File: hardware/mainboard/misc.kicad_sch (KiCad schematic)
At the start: 15 parts

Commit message: More stuff
Signed-off-by: David Shah <dave@ds0.me>
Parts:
- added D? (x2): LED_Small, symbol Device:LED_Small
- added Q?: 2N7002, Package_TO_SOT_SMD:SOT-23, symbol Transistor_FET:2N7002
- added R? (x2): 1k, symbol Device:R_Small
- added R? (x2): 10k, symbol Device:R_Small
- R? (x3): value 1k -> 220
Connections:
- net +3V3: now also R?.1, R?.1, R?.1
- net FLASH_CLK: now also R?.1
- net GND: now also D?.1 (K), Q?.2 (S), R?.2
- new net: D?.2 (A), R?.2 (x2)
- new net: D?.1 (K), Q?.3 (D)
- new net DONE: Q?.1 (G), R?.2
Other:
- moved on the sheet: D?, R?

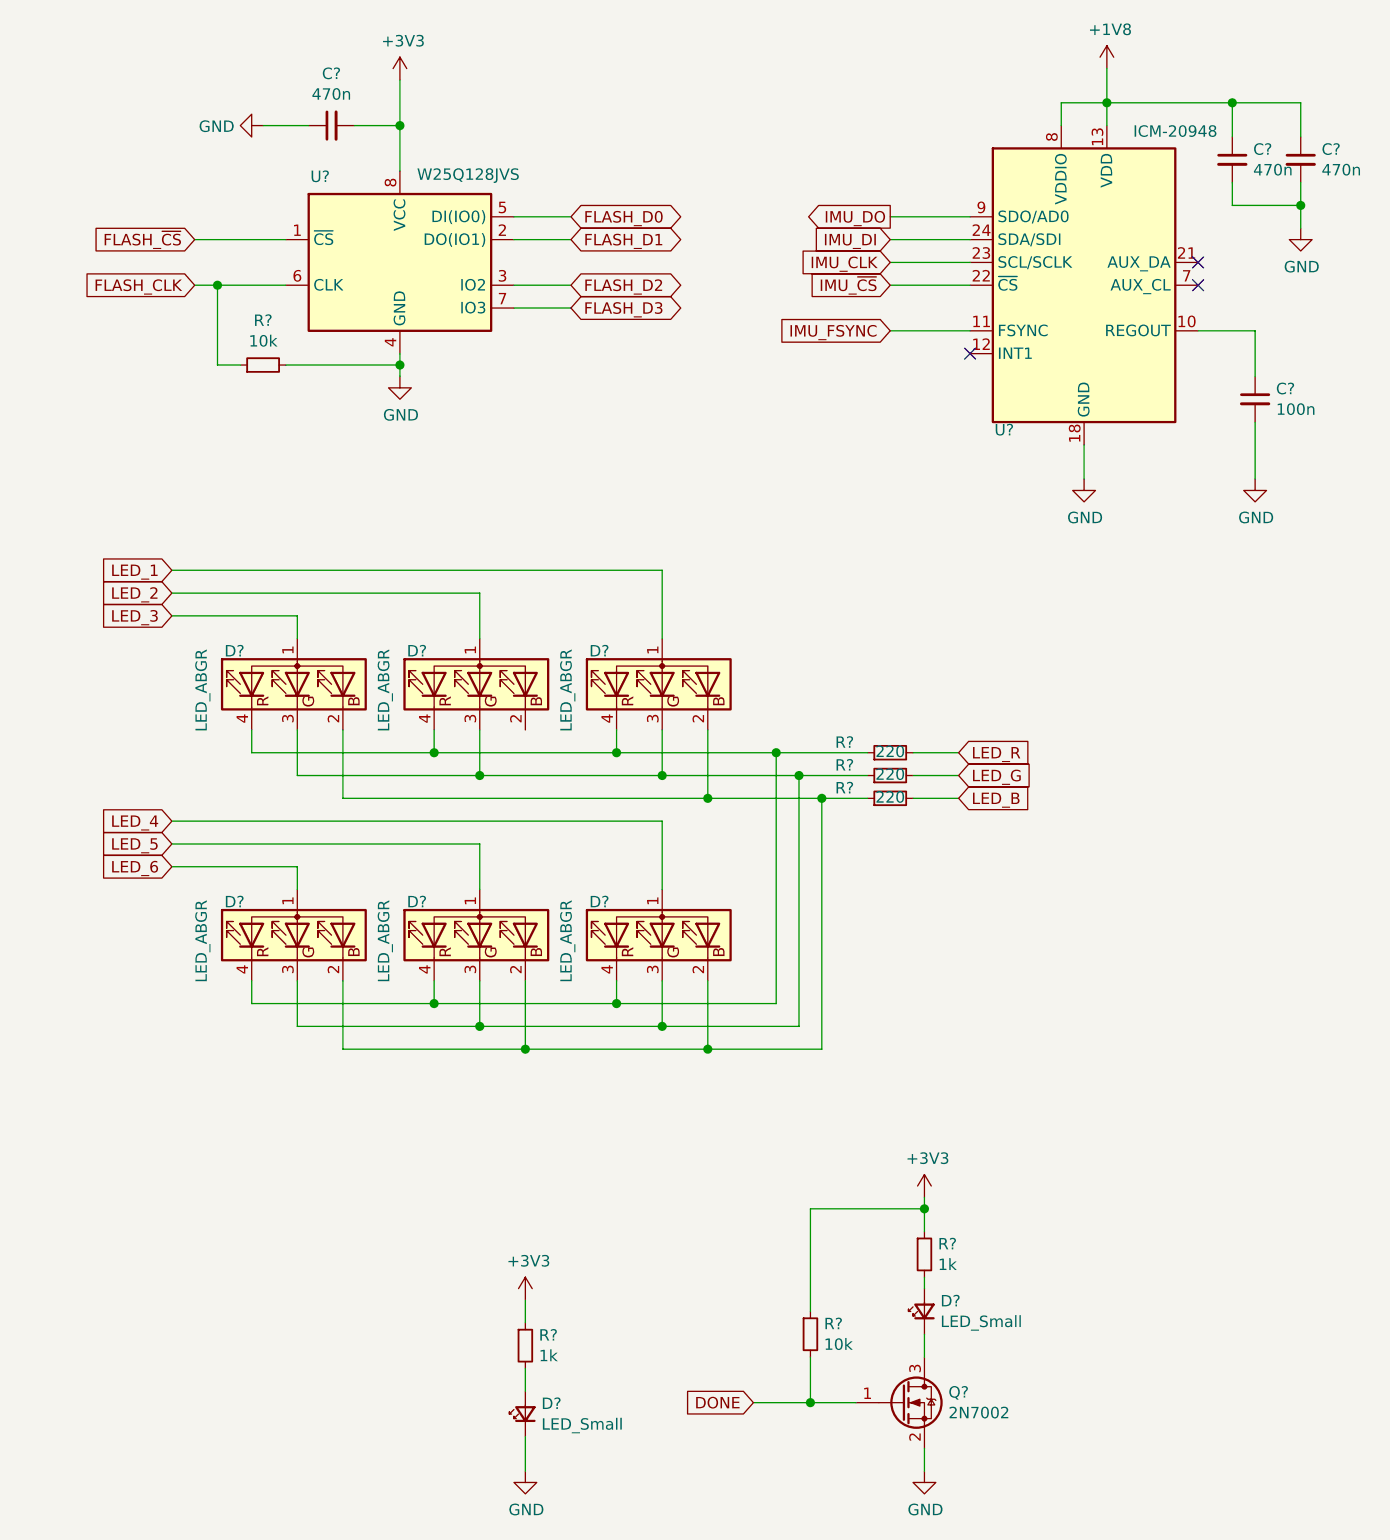
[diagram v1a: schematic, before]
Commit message: Annotate and assign some footpints
Signed-off-by: David Shah <dave@ds0.me>
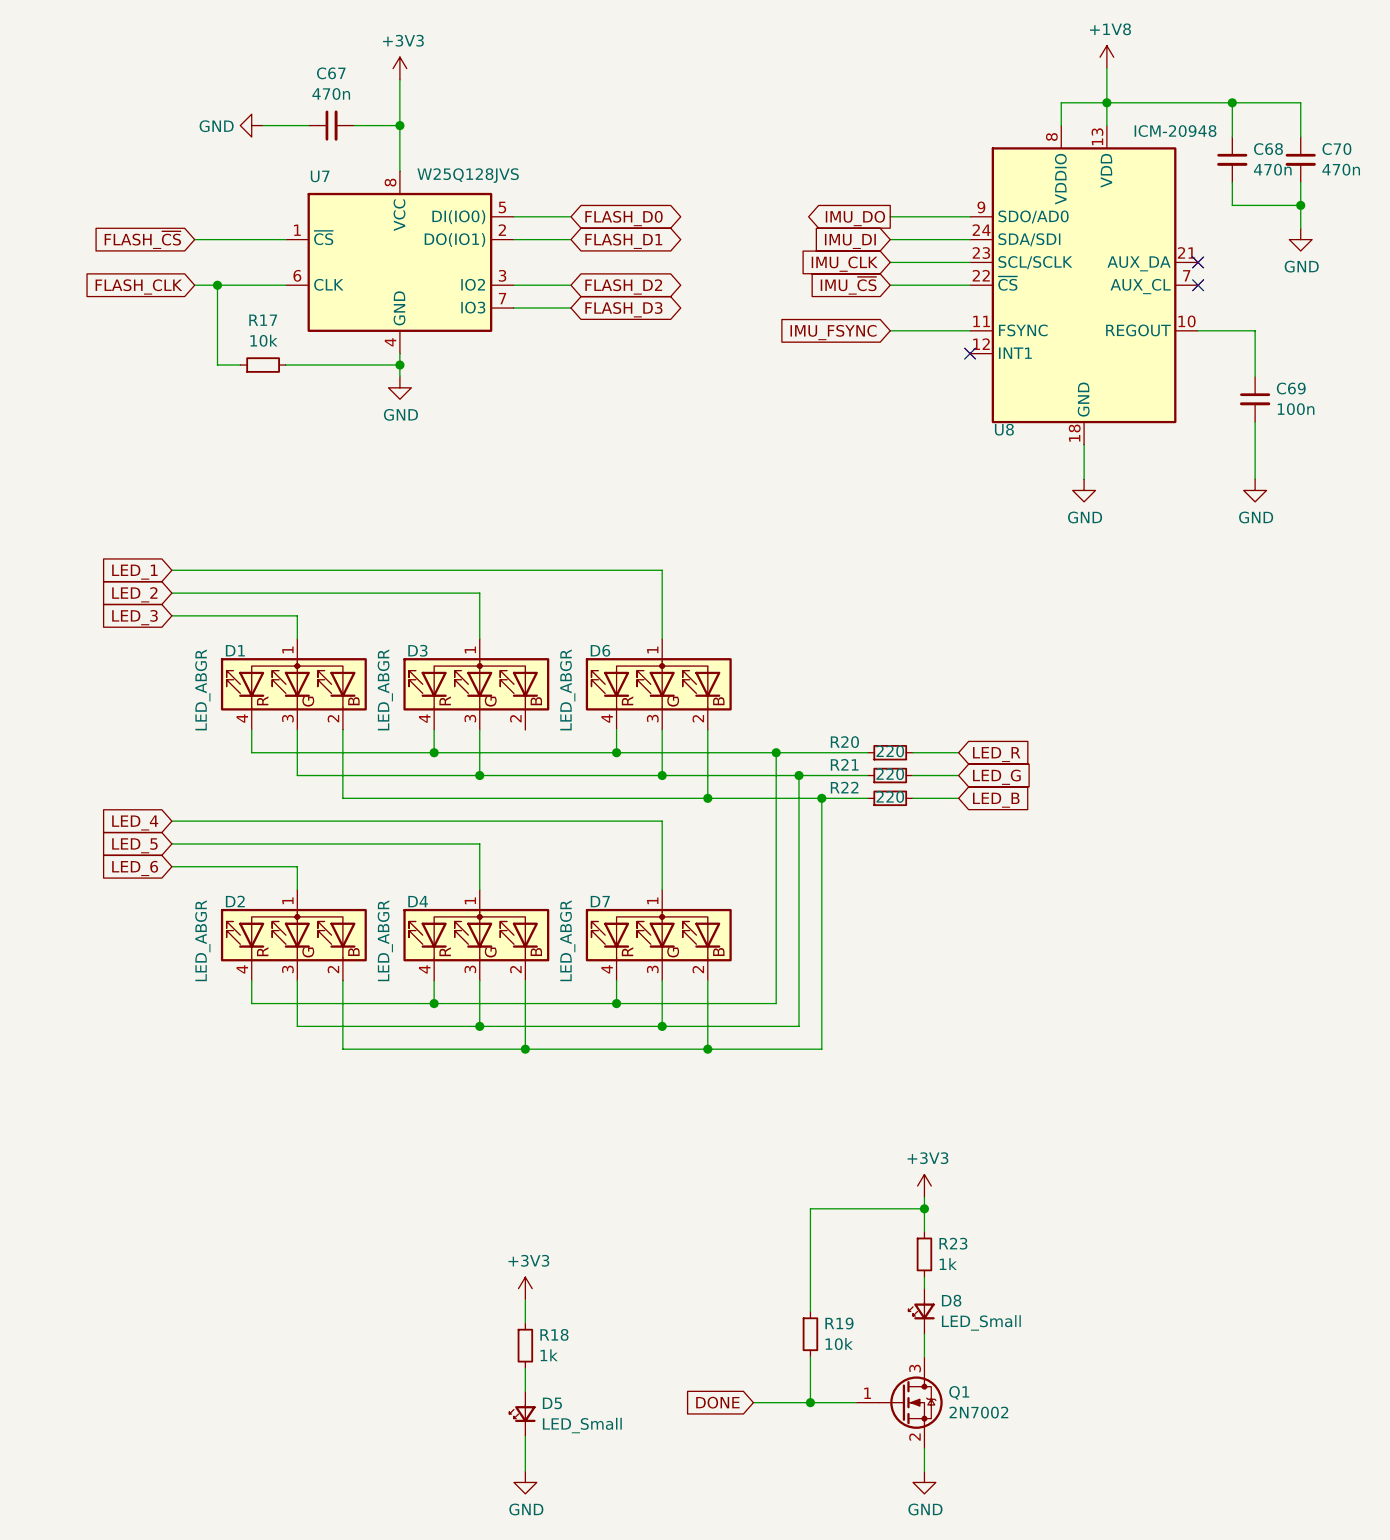
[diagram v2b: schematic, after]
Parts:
- C67, C68, C69, C70: renamed from C?; footprint (none) -> Capacitor_SMD:C_0402_1005Metric
- D1, D2, D3, D4, D6, D7: renamed from D?; footprint (none) -> LED_SMD:LED_Cree-PLCC4_2x2mm_CW
- D5, D8: renamed from D?; footprint (none) -> LED_SMD:LED_0805_2012Metric
- R17, R18, R19, R20, R21, R22, R23: renamed from R?; footprint (none) -> Resistor_SMD:R_0402_1005Metric
- gave numbers to parts that had none: 3

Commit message: First pass at placement
Signed-off-by: David Shah <dave@ds0.me>
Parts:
- added R33: 10k, Resistor_SMD:R_0402_1005Metric, symbol Device:R_Small
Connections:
- net +1V8: now also R33.2
- net IMU_~CS: now also R33.1
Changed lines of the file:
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@@
   (junction (at 118.11 180.34) (diameter 1.016) (color 0 0 0 0))
   (junction (at 119.38 113.03) (diameter 1.016) (color 0 0 0 0))
+  (junction (at 130.81 55.88) (diameter 1.016) (color 0 0 0 0))
   (junction (at 130.81 158.75) (diameter 1.016) (color 0 0 0 0))
+  (junction (at 146.05 35.56) (diameter 1.016) (color 0 0 0 0))
   (junction (at 151.13 35.56) (diameter 1.016) (color 0 0 0 0))
   (junction (at 165.1 35.56) (diameter 1.016) (color 0 0 0 0))
@@
     (stroke (width 0) (type solid) (color 0 0 0 0))
   )
-  (wire (pts (xy 127 55.88) (xy 135.89 55.88))
+  (wire (pts (xy 127 55.88) (xy 130.81 55.88))
     (stroke (width 0) (type solid) (color 0 0 0 0))
   )
@@
     (stroke (width 0) (type solid) (color 0 0 0 0))
   )
+  (wire (pts (xy 130.81 35.56) (xy 130.81 55.88))
+    (stroke (width 0) (type solid) (color 0 0 0 0))
+  )
+  (wire (pts (xy 130.81 55.88) (xy 135.89 55.88))
+    (stroke (width 0) (type solid) (color 0 0 0 0))
+  )
   (wire (pts (xy 130.81 157.48) (xy 130.81 158.75))
     (stroke (width 0) (type solid) (color 0 0 0 0))
@@
     (stroke (width 0) (type solid) (color 0 0 0 0))
   )
+  (wire (pts (xy 134.62 35.56) (xy 130.81 35.56))
+    (stroke (width 0) (type solid) (color 0 0 0 0))
+  )
+  (wire (pts (xy 139.7 35.56) (xy 146.05 35.56))
+    (stroke (width 0) (type solid) (color 0 0 0 0))
+  )
   (wire (pts (xy 146.05 35.56) (xy 146.05 38.1))
     (stroke (width 0) (type solid) (color 0 0 0 0))
   )
+  (wire (pts (xy 146.05 35.56) (xy 151.13 35.56))
+    (stroke (width 0) (type solid) (color 0 0 0 0))
+  )
   (wire (pts (xy 148.59 73.66) (xy 148.59 77.47))
     (stroke (width 0) (type solid) (color 0 0 0 0))
   )
   (wire (pts (xy 151.13 31.75) (xy 151.13 35.56))
-    (stroke (width 0) (type solid) (color 0 0 0 0))
-  )
-  (wire (pts (xy 151.13 35.56) (xy 146.05 35.56))
     (stroke (width 0) (type solid) (color 0 0 0 0))
   )
@@
       (effects (font (size 1.27 1.27)) hide)
     )
+    (pin "1")
+    (pin "2")
+  )
+  (symbol (lib_id "Device:R_Small") (at 137.16 35.56 90) (unit 1)
+    (in_bom yes) (on_board yes)
+    (property "Reference" "R33" (id 0) (at 137.16 30.6132 90))
+    (property "Value" "10k" (id 1) (at 137.16 32.912 90))
+    (property "Footprint" "Resistor_SMD:R_0402_1005Metric" (id 2) (at 137.16 35.56 0)
+      (effects (font (size 1.27 1.27)) hide)
+    )
+    (property "Datasheet" "~" (id 3) (at 137.16 35.56 0)
+      (effects (font (size 1.27 1.27)) hide)
+    )

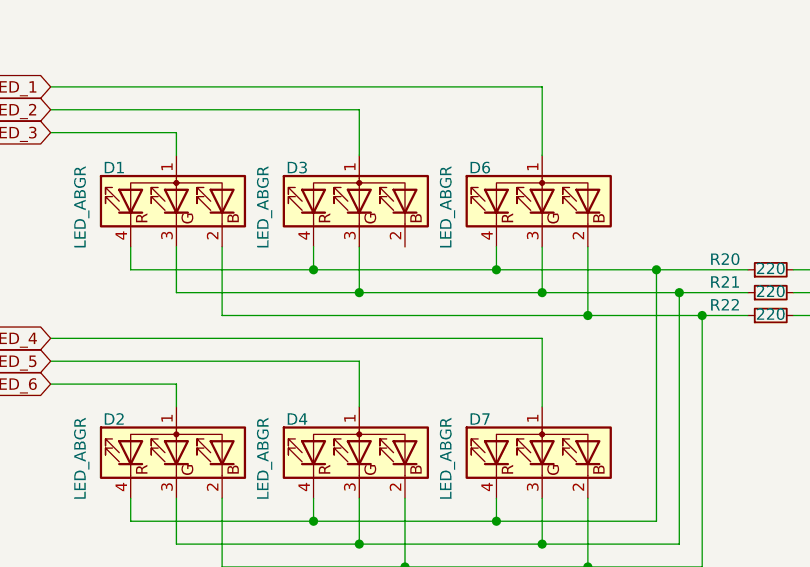
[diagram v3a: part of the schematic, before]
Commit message: mainboard: Fix some schematic ERC issues
Signed-off-by: gatecat <gatecat@ds0.me>
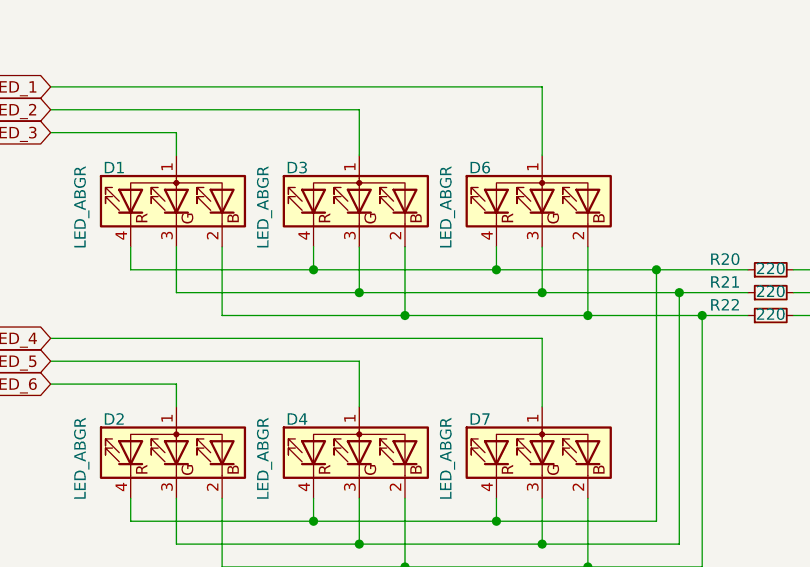
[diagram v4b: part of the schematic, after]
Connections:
- net at D1.2 (BK), D2.2 (BK), D4.2 (BK)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: now also D3.2 (BK)
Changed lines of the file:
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@@
   (junction (at 81.28 110.49) (diameter 1.016) (color 0 0 0 0))
   (junction (at 81.28 138.43) (diameter 1.016) (color 0 0 0 0))
+  (junction (at 86.36 113.03) (diameter 1.016) (color 0 0 0 0))
   (junction (at 86.36 140.97) (diameter 1.016) (color 0 0 0 0))
   (junction (at 96.52 107.95) (diameter 1.016) (color 0 0 0 0))
@@
     (stroke (width 0) (type solid) (color 0 0 0 0))
   )
-  (wire (pts (xy 66.04 113.03) (xy 106.68 113.03))
+  (wire (pts (xy 66.04 113.03) (xy 86.36 113.03))
     (stroke (width 0) (type solid) (color 0 0 0 0))
   )
@@
     (stroke (width 0) (type solid) (color 0 0 0 0))
   )
+  (wire (pts (xy 86.36 105.41) (xy 86.36 113.03))
+    (stroke (width 0) (type solid) (color 0 0 0 0))
+  )
+  (wire (pts (xy 86.36 113.03) (xy 106.68 113.03))
+    (stroke (width 0) (type solid) (color 0 0 0 0))
+  )

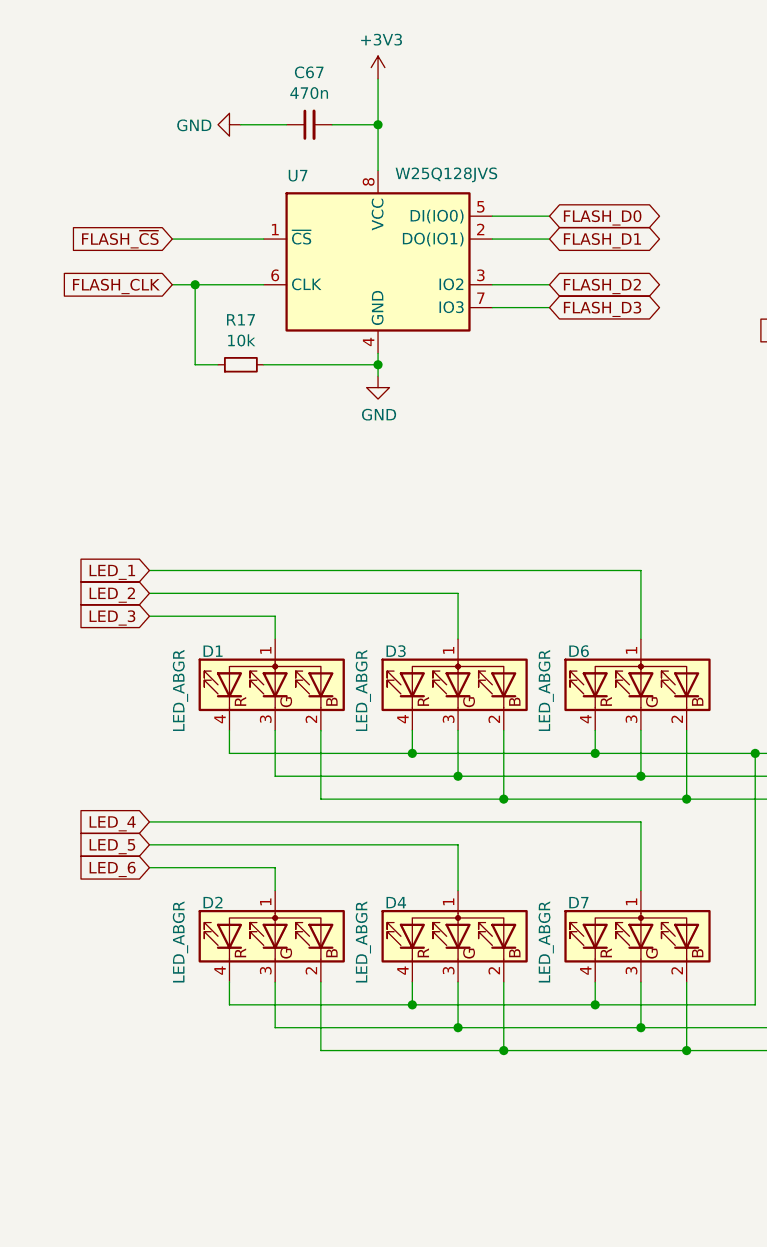
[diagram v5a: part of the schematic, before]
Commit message: Update some part numbers
Signed-off-by: gatecat <gatecat@ds0.me>
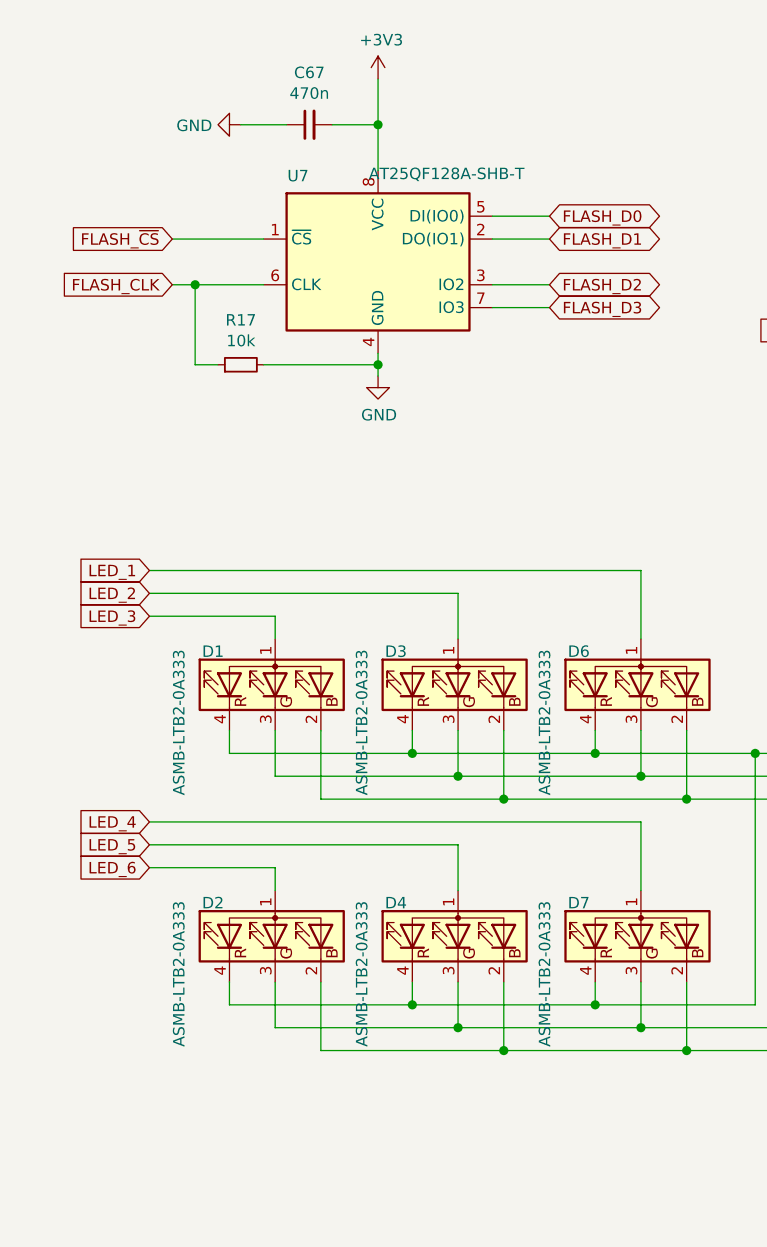
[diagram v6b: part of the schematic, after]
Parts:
- D1, D2, D3, D4, D6, D7: value LED_ABGR -> ASMB-LTB2-0A333
- U7: value W25Q128JVS -> AT25QF128A-SHB-T
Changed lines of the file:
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@@
       (effects (font (size 1.27 1.27)) (justify right))
     )
-    (property "Value" "LED_ABGR" (id 1) (at 50.2921 96.3993 0)
+    (property "Value" "ASMB-LTB2-0A333" (id 1) (at 50.2921 96.3993 0)
       (effects (font (size 1.27 1.27)) (justify right))
     )
@@
       (effects (font (size 1.27 1.27)) (justify right))
     )
-    (property "Value" "LED_ABGR" (id 1) (at 50.2921 124.3393 0)
+    (property "Value" "ASMB-LTB2-0A333" (id 1) (at 50.2921 124.3393 0)
       (effects (font (size 1.27 1.27)) (justify right))
     )
@@
       (effects (font (size 1.27 1.27)) (justify right))
     )
-    (property "Value" "LED_ABGR" (id 1) (at 70.6121 96.3993 0)
+    (property "Value" "ASMB-LTB2-0A333" (id 1) (at 70.6121 96.3993 0)
       (effects (font (size 1.27 1.27)) (justify right))
     )
@@
       (effects (font (size 1.27 1.27)) (justify right))
     )
-    (property "Value" "LED_ABGR" (id 1) (at 70.6121 124.3393 0)
+    (property "Value" "ASMB-LTB2-0A333" (id 1) (at 70.6121 124.3393 0)
       (effects (font (size 1.27 1.27)) (justify right))
     )
@@
       (effects (font (size 1.27 1.27)) (justify right))
     )
-    (property "Value" "LED_ABGR" (id 1) (at 90.9321 96.3993 0)
+    (property "Value" "ASMB-LTB2-0A333" (id 1) (at 90.9321 96.3993 0)
       (effects (font (size 1.27 1.27)) (justify right))
     )
@@
       (effects (font (size 1.27 1.27)) (justify right))
     )
-    (property "Value" "LED_ABGR" (id 1) (at 90.9321 124.3393 0)
+    (property "Value" "ASMB-LTB2-0A333" (id 1) (at 90.9321 124.3393 0)
       (effects (font (size 1.27 1.27)) (justify right))
     )
@@
     (in_bom yes) (on_board yes)
     (property "Reference" "U7" (id 0) (at 63.5 43.7958 0))
-    (property "Value" "W25Q128JVS" (id 1) (at 80.01 43.5545 0))
+    (property "Value" "AT25QF128A-SHB-T" (id 1) (at 80.01 43.5545 0))
     (property "Footprint" "Package_SO:SOIC-8_5.23x5.23mm_P1.27mm" (id 2) (at 72.39 53.34 0)
       (effects (font (size 1.27 1.27)) hide)
